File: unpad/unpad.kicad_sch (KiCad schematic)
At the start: 12 parts, among them SW1 RotaryEncoder_Switch, U1 RP2040, U24 W25Q16JVSSIQ, Y2 RH100-12.000-18-2030-TR

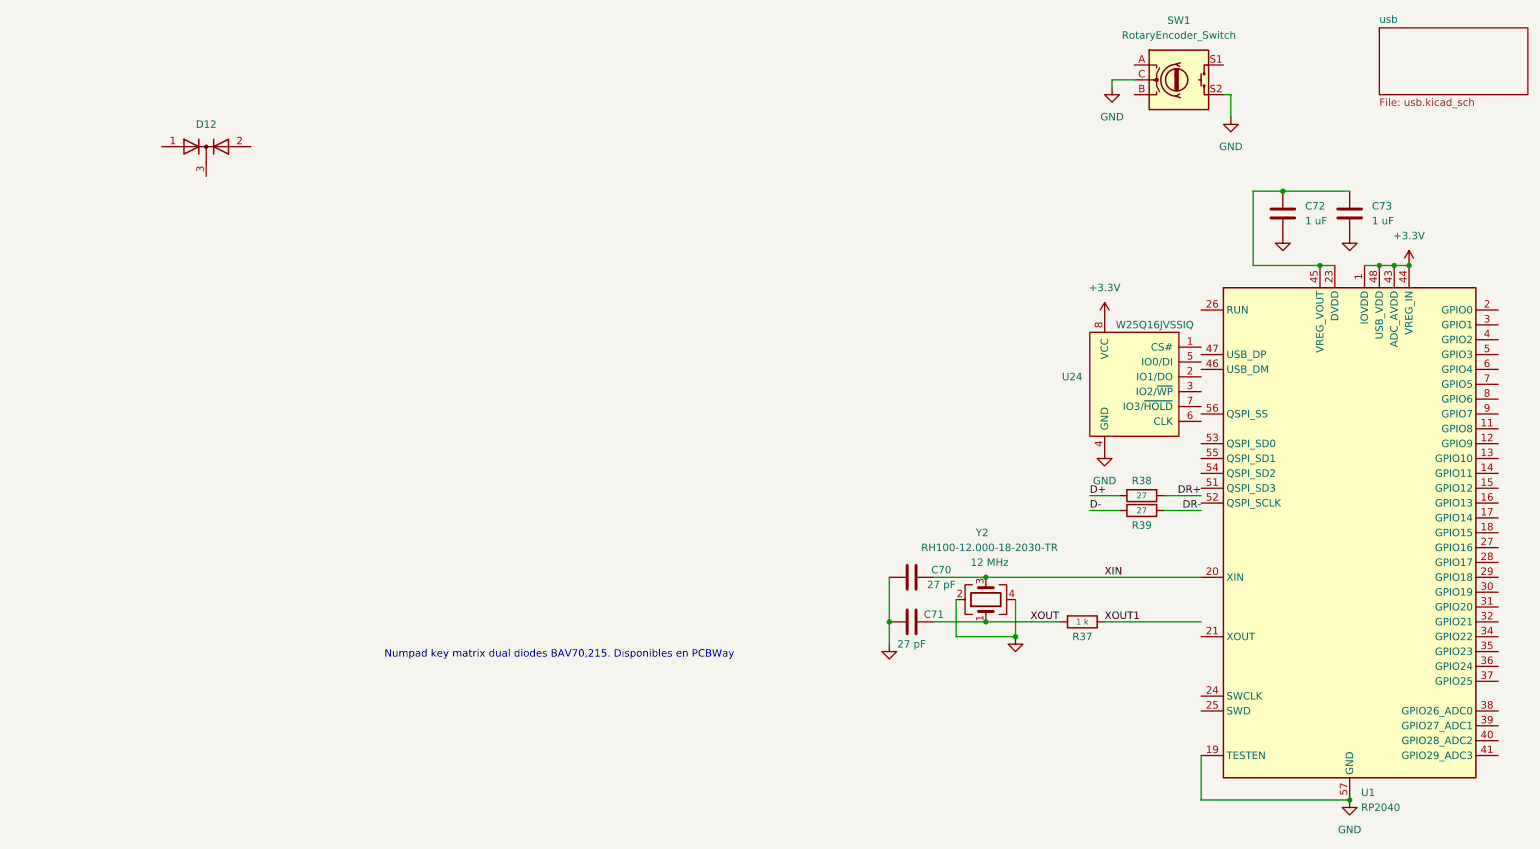
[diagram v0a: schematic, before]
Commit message: ADD: esquemático del numpad para las teclas solo
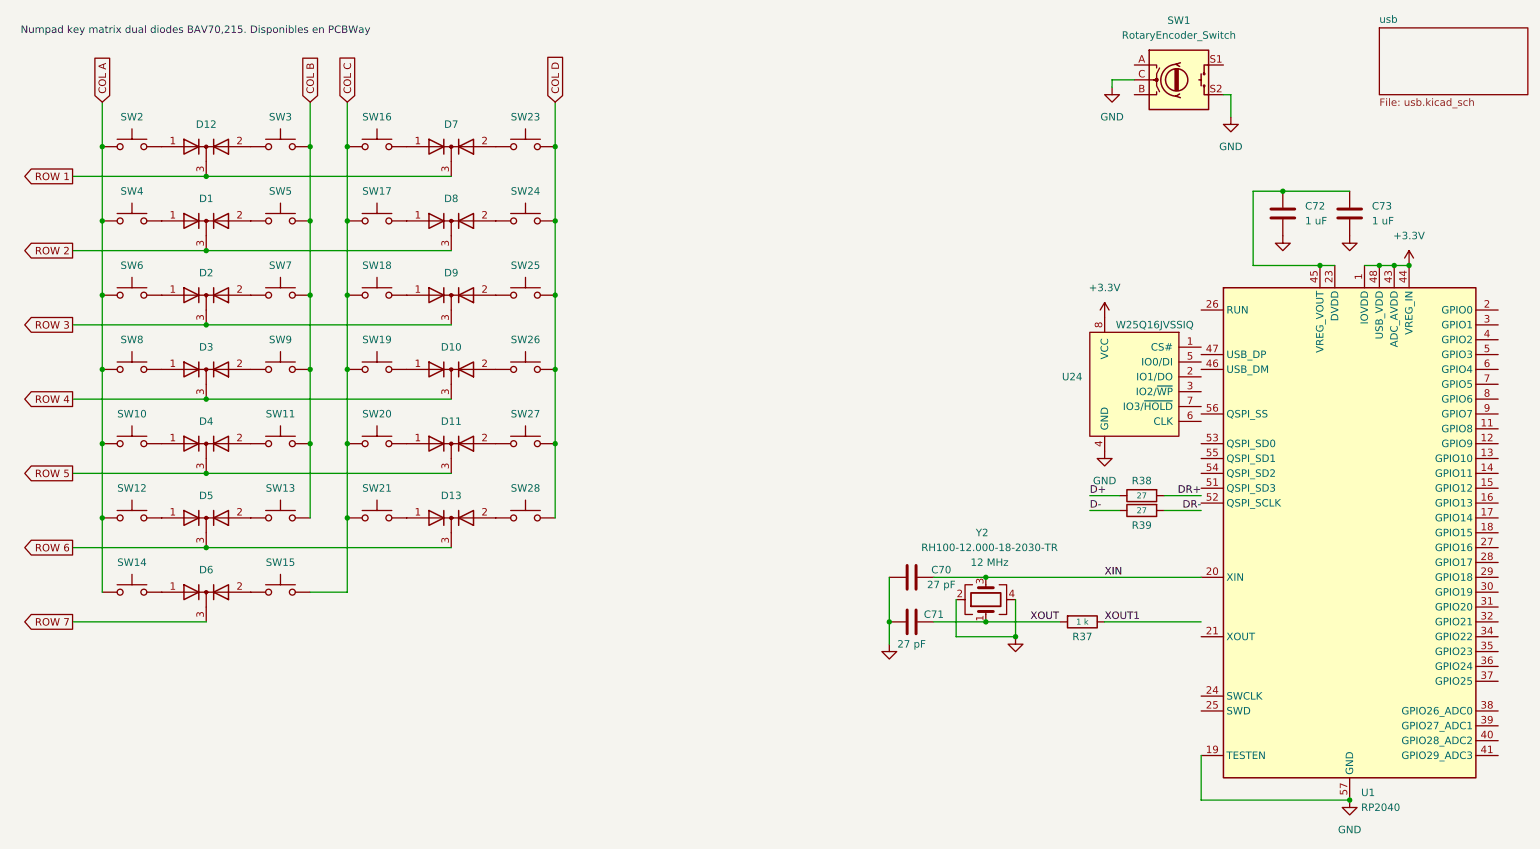
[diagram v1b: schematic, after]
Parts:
- added D1, D10, D11, D13, D2, D3, D4, D5, D6, D7, D8, D9: BAV70, Package_TO_SOT_SMD:SOT-23, symbol Diode:BAV70
- added SW10, SW11, SW12, SW13, SW14, SW15, SW16, SW17, SW18, SW19, SW2, SW20, SW21, SW23, SW24, SW25, SW26, SW27, SW28, SW3, SW4, SW5, SW6, SW7, SW8, SW9: SW_Cherry_MX, PCM_Switch_Keyboard_Cherry_MX:SW_Cherry_MX_PCB, symbol unkeyboard:SW_Cherry_MX
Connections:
- net at D12.1 (A): now also SW2.2
- net at D12.2 (A): now also SW3.1
- net ROW 1: now reaches D12.3 (K)
- net ROW 1: now also D7.3 (K)
- new net: D4.1 (A), SW10.2
- new net: D8.1 (A), SW17.2
- new net: D11.1 (A), SW20.2
- new net: D11.2 (A), SW27.1
- new net: D2.2 (A), SW7.1
- new net: D9.1 (A), SW18.2
- new net: D9.2 (A), SW25.1
- new net: D5.1 (A), SW12.2
- new net: D2.1 (A), SW6.2
- new net: D6.2 (A), SW15.1
- new net: D6.1 (A), SW14.2
- new net: D8.2 (A), SW24.1
- new net: D7.1 (A), SW16.2
- new net: D7.2 (A), SW23.1
- new net: D13.2 (A), SW28.1
- new net: D4.2 (A), SW11.1
- new net: D1.2 (A), SW5.1
- new net: D5.2 (A), SW13.1
- new net: D10.2 (A), SW26.1
- new net: D13.1 (A), SW21.2
- new net: D3.2 (A), SW9.1
- new net: D1.1 (A), SW4.2
- new net: D10.1 (A), SW19.2
- new net: D3.1 (A), SW8.2
- new net COL A: SW10.1, SW12.1, SW14.1, SW2.1, SW4.1, SW6.1, SW8.1
- new net COL B: SW11.2, SW13.2, SW3.2, SW5.2, SW7.2, SW9.2
- new net COL C: SW15.2, SW16.1, SW17.1, SW18.1, SW19.1, SW20.1, SW21.1
- new net COL D: SW23.2, SW24.2, SW25.2, SW26.2, SW27.2, SW28.2
- new net ROW 2: D1.3 (K), D8.3 (K)
- new net ROW 3: D2.3 (K), D9.3 (K)
- new net ROW 4: D10.3 (K), D3.3 (K)
- new net ROW 5: D11.3 (K), D4.3 (K)
- new net ROW 6: D13.3 (K), D5.3 (K)
- new net ROW 7: D6.3 (K)
